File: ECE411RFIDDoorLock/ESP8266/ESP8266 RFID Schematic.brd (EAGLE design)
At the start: 61 x 43.8 mm, 30 parts, among them M1 SERVO, Q3 DMG341, T1 600mA/40V, T2 600mA/40V, U3 AP2112-3.3, X1 ESP-12E, X4 20329

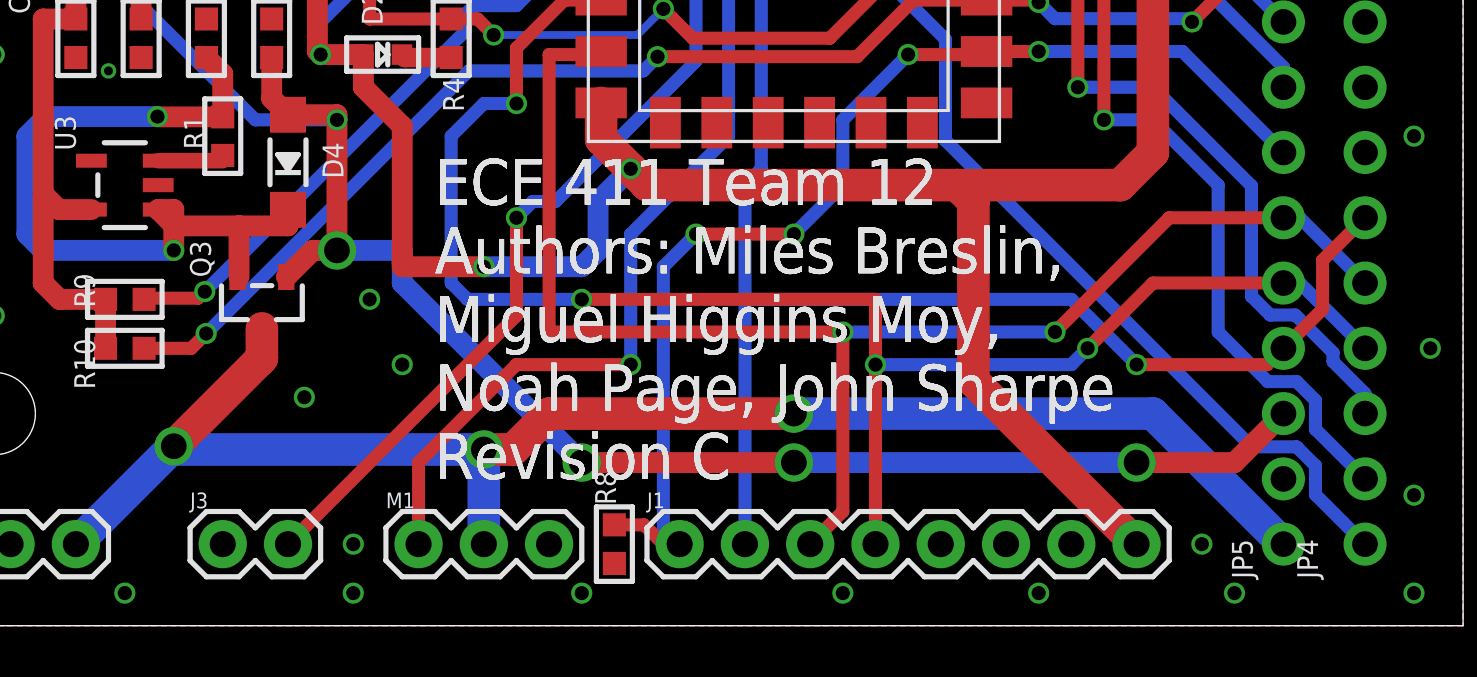
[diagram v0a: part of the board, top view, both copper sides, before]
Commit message: routed EN
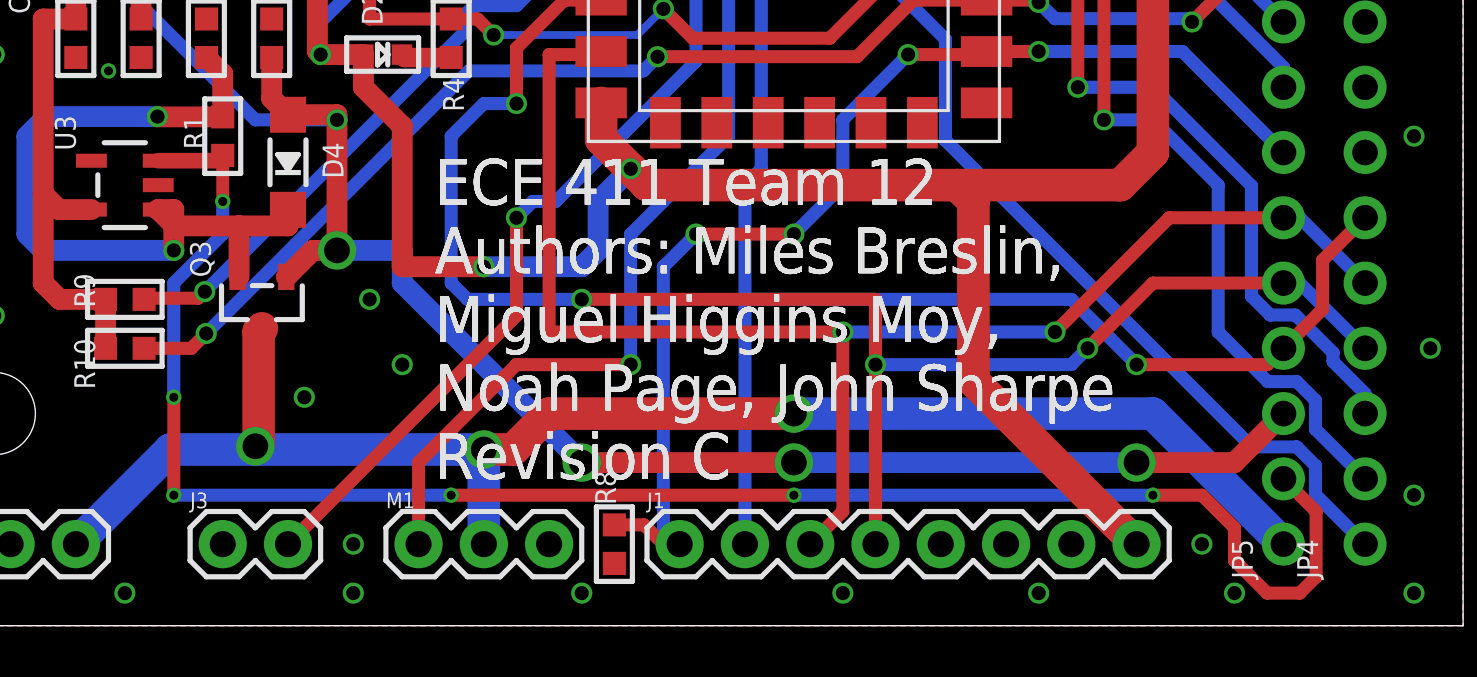
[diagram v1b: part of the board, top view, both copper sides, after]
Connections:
- removed net N$10: R1.1, U3.3
- net EN: now also R1.1, U3.3
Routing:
- net EN: track 0.00 -> 67.9 mm, vias 0 -> 6
- net N$10: track 2.71 -> 0.00 mm
- net VBAT: track 61.0 -> 59.7 mm
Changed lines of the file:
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@@
 <contactref element="J2" pad="2"/>
 <wire x1="6.985" y1="3.175" x2="10.668" y2="6.858" width="1.27" layer="16"/>
-<wire x1="10.668" y1="6.858" x2="10.795" y2="6.858" width="1.27" layer="16"/>
-<wire x1="10.795" y1="6.858" x2="22.86" y2="6.858" width="1.27" layer="16"/>
+<wire x1="10.668" y1="6.858" x2="13.97" y2="6.858" width="1.27" layer="16"/>
+<wire x1="13.97" y1="6.858" x2="22.86" y2="6.858" width="1.27" layer="16"/>
 <wire x1="22.86" y1="6.858" x2="22.86" y2="3.175" width="1.27" layer="16"/>
 <via x="22.86" y="6.858" extent="1-16" drill="1"/>
@@
 <wire x1="48.895" y1="8.255" x2="34.925" y2="8.255" width="1.27" layer="16"/>
 <wire x1="48.895" y1="8.255" x2="53.975" y2="3.175" width="1.27" layer="16"/>
-<via x="10.795" y="6.985" extent="1-16" drill="1"/>
-<wire x1="10.795" y1="6.985" x2="10.795" y2="6.858" width="1.27" layer="16"/>
-<wire x1="10.795" y1="6.985" x2="14.097" y2="10.287" width="1.27" layer="1"/>
-<wire x1="14.097" y1="10.287" x2="14.224" y2="10.414" width="1.27" layer="1"/>
-<wire x1="14.224" y1="10.414" x2="14.224" y2="11.573" width="1.27" layer="1"/>
+<via x="13.97" y="6.985" extent="1-16" drill="1"/>
+<wire x1="13.97" y1="6.985" x2="13.97" y2="6.858" width="1.27" layer="16"/>
+<wire x1="14.097" y1="7.112" x2="13.97" y2="6.985" width="1.27" layer="1"/>
+<wire x1="14.097" y1="11.446" x2="14.097" y2="7.112" width="1.27" layer="1"/>
+<wire x1="14.097" y1="11.446" x2="14.224" y2="11.573" width="1.27" layer="1"/>
 </signal>
 <signal name="VBUS" class="1">
@@
 <wire x1="13.335" y1="13.573" x2="13.335" y2="15.56" width="0.8128" layer="1"/>
 </signal>
-<signal name="N$10">
-<contactref element="U3" pad="3"/>
-<contactref element="R1" pad="1"/>
-<wire x1="10.1901" y1="18.095" x2="12.7" y2="18.095" width="0.6096" layer="1"/>
-<wire x1="12.7" y1="18.095" x2="12.7" y2="18.3" width="0.3048" layer="1"/>
-</signal>
 <signal name="N$14">
 <contactref element="C4" pad="1"/>
@@
 <signal name="EN">
 <contactref element="JP5" pad="2"/>
+<contactref element="U3" pad="3"/>
+<contactref element="R1" pad="1"/>
+<wire x1="10.1901" y1="18.095" x2="12.7" y2="18.095" width="0.6096" layer="1"/>
+<wire x1="12.7" y1="18.095" x2="12.7" y2="18.3" width="0.3048" layer="1"/>
+<wire x1="53.975" y1="5.715" x2="55.245" y2="4.445" width="0.508" layer="1"/>
+<wire x1="55.245" y1="4.445" x2="55.245" y2="1.905" width="0.508" layer="1"/>
+<wire x1="55.245" y1="1.905" x2="54.61" y2="1.27" width="0.508" layer="1"/>
+<wire x1="54.61" y1="1.27" x2="53.34" y2="1.27" width="0.508" layer="1"/>
+<wire x1="53.34" y1="1.27" x2="52.07" y2="2.54" width="0.508" layer="1"/>
+<wire x1="52.07" y1="2.54" x2="52.07" y2="3.81" width="0.508" layer="1"/>
+<wire x1="52.07" y1="3.81" x2="50.8" y2="5.08" width="0.508" layer="1"/>
+<wire x1="50.8" y1="5.08" x2="48.895" y2="5.08" width="0.508" layer="1"/>
+<via x="48.895" y="5.08" extent="1-16" drill="0.35"/>
+<wire x1="48.895" y1="5.08" x2="34.925" y2="5.08" width="0.508" layer="16"/>
+<via x="34.925" y="5.08" extent="1-16" drill="0.35"/>
+<wire x1="34.925" y1="5.08" x2="21.59" y2="5.08" width="0.508" layer="1"/>
+<via x="21.59" y="5.08" extent="1-16" drill="0.35"/>
+<wire x1="21.59" y1="5.08" x2="10.795" y2="5.08" width="0.508" layer="16"/>
+<via x="10.795" y="5.08" extent="1-16" drill="0.35"/>
+<wire x1="10.795" y1="5.08" x2="10.795" y2="8.89" width="0.508" layer="1"/>
+<via x="10.795" y="8.89" extent="1-16" drill="0.35"/>
+<wire x1="10.795" y1="8.89" x2="10.795" y2="13.335" width="0.508" layer="16"/>
+<wire x1="12.7" y1="15.24" x2="12.7" y2="16.51" width="0.508" layer="16"/>
+<via x="12.7" y="16.51" extent="1-16" drill="0.35"/>
+<wire x1="12.7" y1="16.51" x2="12.7" y2="18.095" width="0.508" layer="1"/>
+<wire x1="10.795" y1="13.335" x2="12.7" y2="15.24" width="0.508" layer="16"/>
 </signal>
 </signals>

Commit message: Some VIA work and clean up
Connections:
- removed net TP: U1.THERM
- net GND: now also U1.THERM
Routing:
- net EN: track 67.9 -> 60.0 mm
- net 3.3V: track 130.2 -> 128.8 mm
- net GPIO0: track 44.1 -> 43.1 mm
- net GND: track 3.52 -> 4.45 mm, vias 46 -> 65
- net GPIO12/MISO: track 62.7 -> 63.2 mm
- net VBUS: track 81.8 -> 81.3 mm
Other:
- board text added: "ECE 411 Team 12 Authors: Miles Breslin, Miguel Higgins Moy, Noah Page, John Sharpe Revision C Adapted from Adafruit Feather Huzzah by Limor Fried/Ladyada for Adafruit Industries"
- board text removed: "ECE 411 Team 12 Authors: Miles Breslin, Miguel Higgins Moy, Noah Page, John Sharpe Revision C"

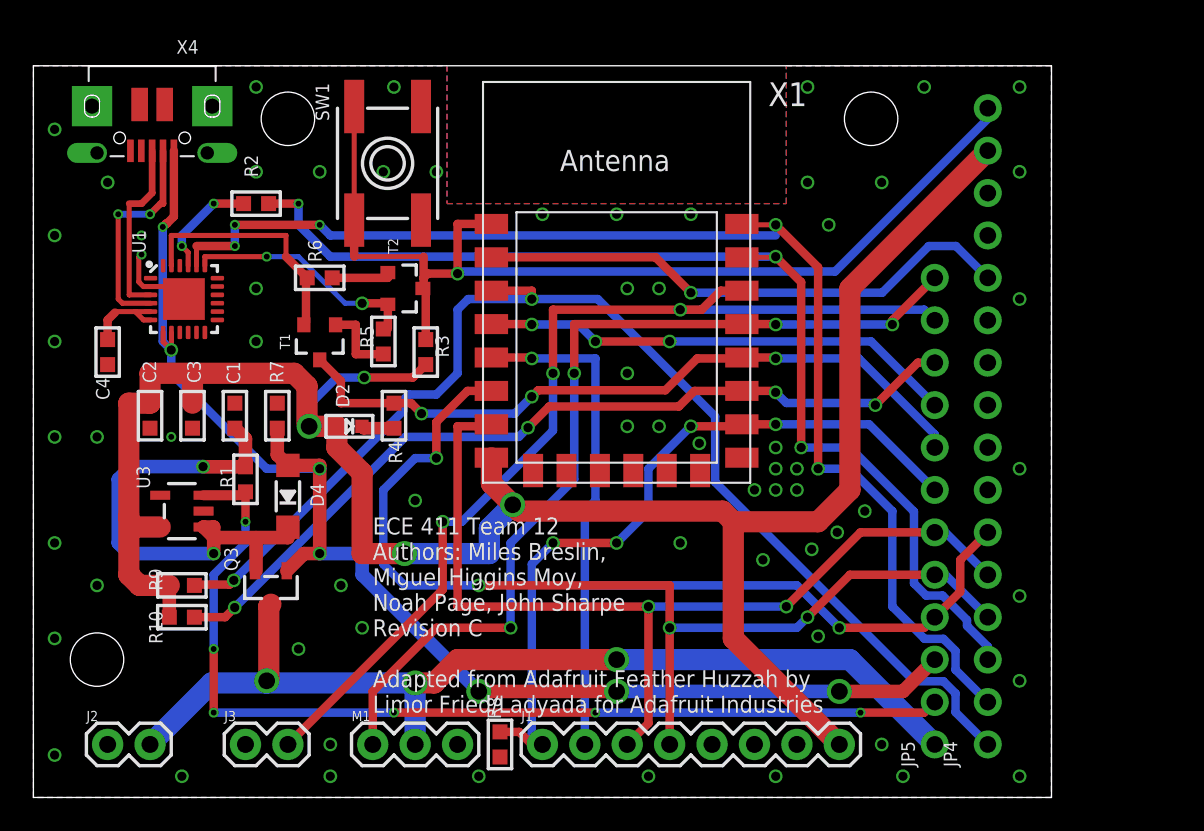
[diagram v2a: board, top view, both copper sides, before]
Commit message: Design review feedback changed, USB replaced add new library
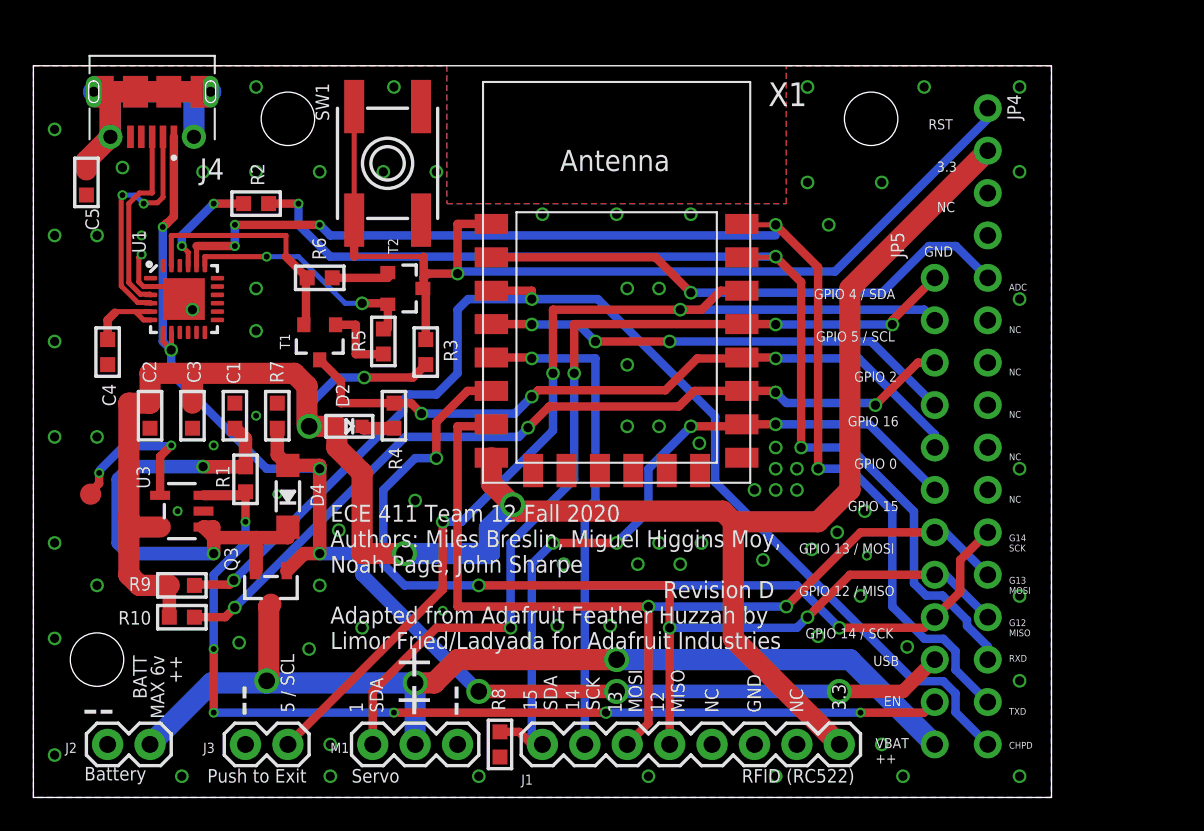
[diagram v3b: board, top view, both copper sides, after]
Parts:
- removed X4: 20329, microbuilder:4UCONN_20329_V2
- added C5: 100n, microbuilder:0603-MINI
- added J4: 1050170001, 1050170001:MOLEX_1050170001
- added TP1: TEST-POINT3X5, SparkFun-Connectors:PAD.03X.05
- D2: value (none) -> RED
- SW1: value (none) -> BB3S-1000
- U1: value (none) -> CP2104
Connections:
- new net N$1: C5.1, J4.SH1, J4.SH2, J4.SH3, J4.SH4, J4.SH5, J4.SH6, J4.SH7, J4.SH8
- new net N$2: J4.3, U1.3
- net GND: now also C5.2, J4.5; no longer X4.BASE@1, X4.BASE@2, X4.GND, X4.SPRT@1, X4.SPRT@2, X4.SPRT@3, X4.SPRT@4
- net N$3: now also J4.2, U1.4; no longer U1.3, X4.D+
- net N$4: now also TP1.P$1, U3.4; no longer U1.4, X4.D-
- net VBUS: now also J4.1; no longer X4.VBUS
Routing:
- net N$1: track 0.00 -> 25.9 mm
- net N$2: track 0.00 -> 11.4 mm
- net N$4: track 13.2 -> 9.82 mm
- net N$3: track 10.9 -> 14.1 mm, vias 0 -> 2
- net VBUS: track 81.3 -> 82.1 mm
- net GND: track 4.45 -> 5.14 mm, vias 65 -> 84
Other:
- board text added: "++"
- board text added: "--"
- board text added: "1 SDA"
- board text added: "12 MISO"
- board text added: "13 MOSI"
- board text added: "14 SCK"
- board text added: "15 SDA"
- board text added: "3.3"
- board text added: "5 / SCL"
- board text added: "ADC"
- board text added: "BATT MAX 6v ++"
- board text added: "Battery"
- board text added: "CHPD"
- board text added: "ECE 411 Team 12 Fall 2020 Authors: Miles Breslin, Miguel Higgins Moy, Noah Page, John Sharpe Revision D Adapted from Adafruit Feather Huzzah by Limor Fried/Ladyada for Adafruit Industries"
- board text added: "EN"
- board text added: "G12 MISO"
- board text added: "G13 MOSI"
- board text added: "G14 SCK"
- board text added: "GND"
- board text added: "GPIO 0"
- board text added: "GPIO 12 / MISO"
- board text added: "GPIO 13 / MOSI"
- board text added: "GPIO 14 / SCK"
- board text added: "GPIO 15"
- board text added: "GPIO 16"
- board text added: "GPIO 2"
- board text added: "GPIO 4 / SDA"
- board text added: "GPIO 5 / SCL"
- board text added: "NC"
- board text added: "Push to Exit"
- board text added: "RFID (RC522)"
- board text added: "RST"
- board text added: "RXD"
- board text added: "Servo"
- board text added: "TXD"
- board text added: "USB"
- board text added: "VBAT ++"
- board text removed: "ECE 411 Team 12 Authors: Miles Breslin, Miguel Higgins Moy, Noah Page, John Sharpe Revision C Adapted from Adafruit Feather Huzzah by Limor Fried/Ladyada for Adafruit Industries"

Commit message: PCB Clean Up from Design Review
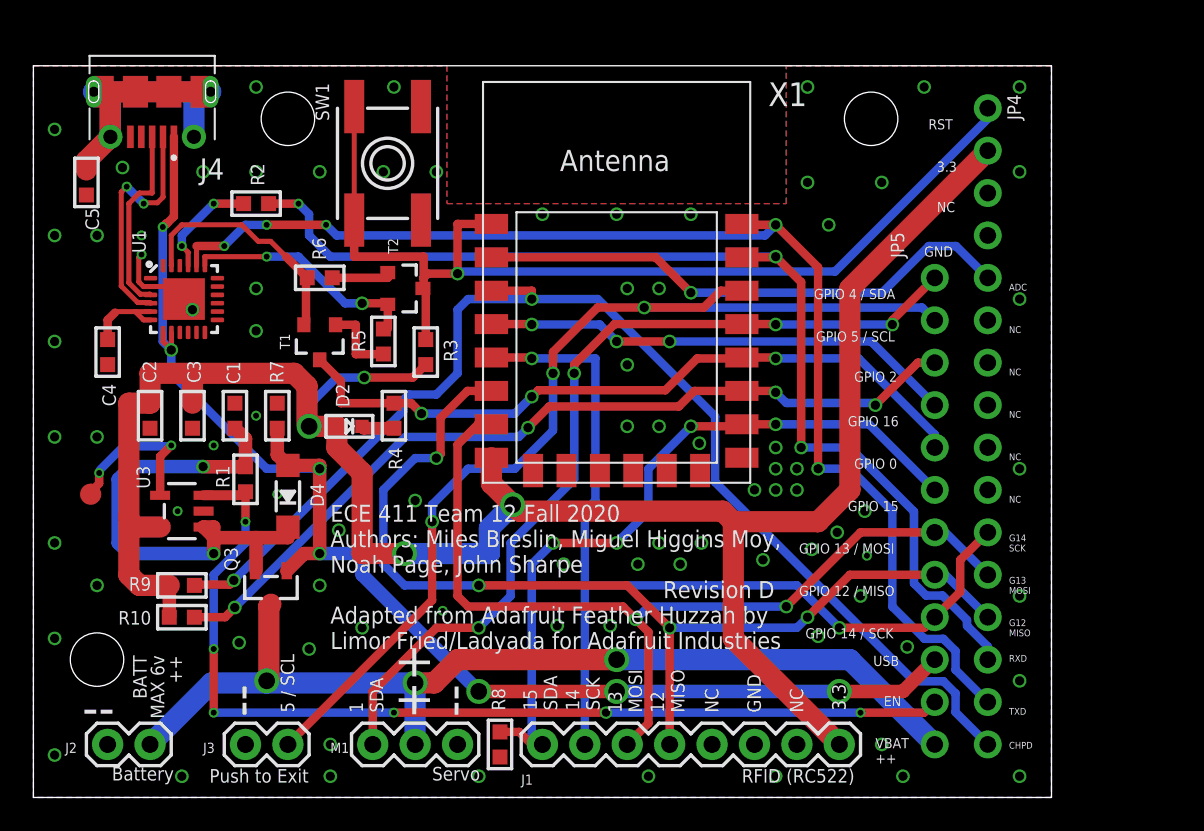
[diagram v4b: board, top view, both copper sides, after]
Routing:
- net GPIO4/SDA: track 55.7 -> 53.1 mm
- net GPIO5/SCL: track 60.6 -> 62.3 mm
- net GPIO12/MISO: track 63.2 -> 61.8 mm
- net TXD: track 75.7 -> 74.6 mm
- net GPIO13/MOSI: track 56.4 -> 55.6 mm
- net N$3: track 14.1 -> 14.6 mm

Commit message: Final PCB Draft, some component modifications, please take a look.
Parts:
- removed SW1: BB3S-1000, microbuilder:EVQ-Q2
- removed TP1: TEST-POINT3X5, SparkFun-Connectors:PAD.03X.05
- removed U3: AP2112-3.3, microbuilder:SOT23-5
- added S1: B3S-1000, B3S-1000:SW_B3S-1000
- added U2: AP2112K-3.3TRG1, AP2112K-3.3TRG1:SOT95P285X140-5N
- D4: value MBR0540 -> MBR140SFT1G
- Q3: value DMG341 -> MMBT2222ALT1GOSCT-ND
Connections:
- removed net N$4: TP1.P$1, U3.4
- net 3.3V: now also U2.5; no longer U3.5
- net EN: now also U2.3; no longer U3.3
- net GND: now also S1.1, S1.2, U2.2; no longer SW1.A, SW1.A', U3.2
- net N$8: now also U2.1; no longer U3.1
- net RESET: now also S1.3, S1.4; no longer SW1.B, SW1.B'
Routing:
- net N$4: track 9.82 -> 0.00 mm, vias 2 -> 0
- net EN: track 60.0 -> 60.5 mm
- net GND: vias 84 -> 98
